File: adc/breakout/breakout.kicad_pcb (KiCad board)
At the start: 2 copper layers, 34.4 x 22.1 mm, 52 parts, among them J1 Conn_01x05_Pin, J2 Conn_01x05_Pin, J3 Conn_01x03_Pin, J4 Conn_01x06_Pin, U1 ESD5344D-TP, U2 ADS1261IRHBR, U3 ESD5344D-TP, U4 ESD5344D-TP

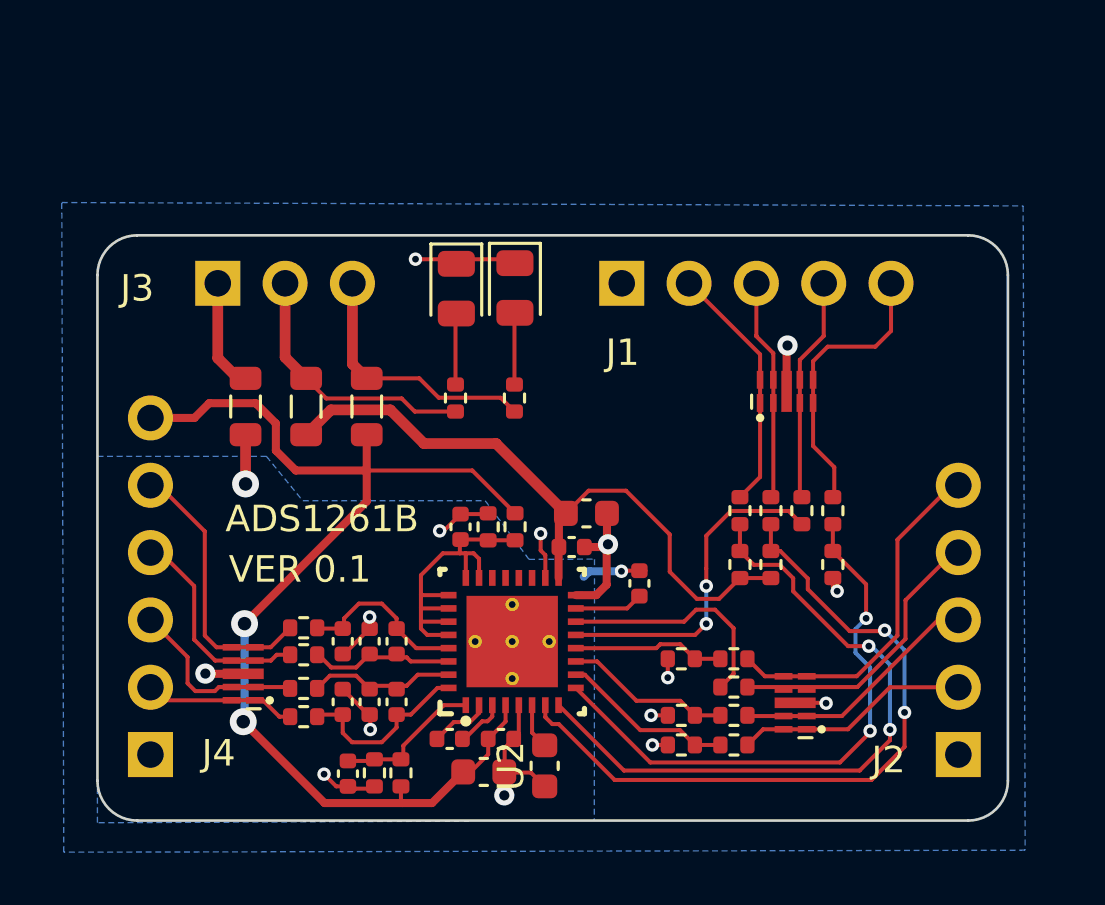
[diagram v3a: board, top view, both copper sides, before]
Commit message: Completed the layout of the power supplies.
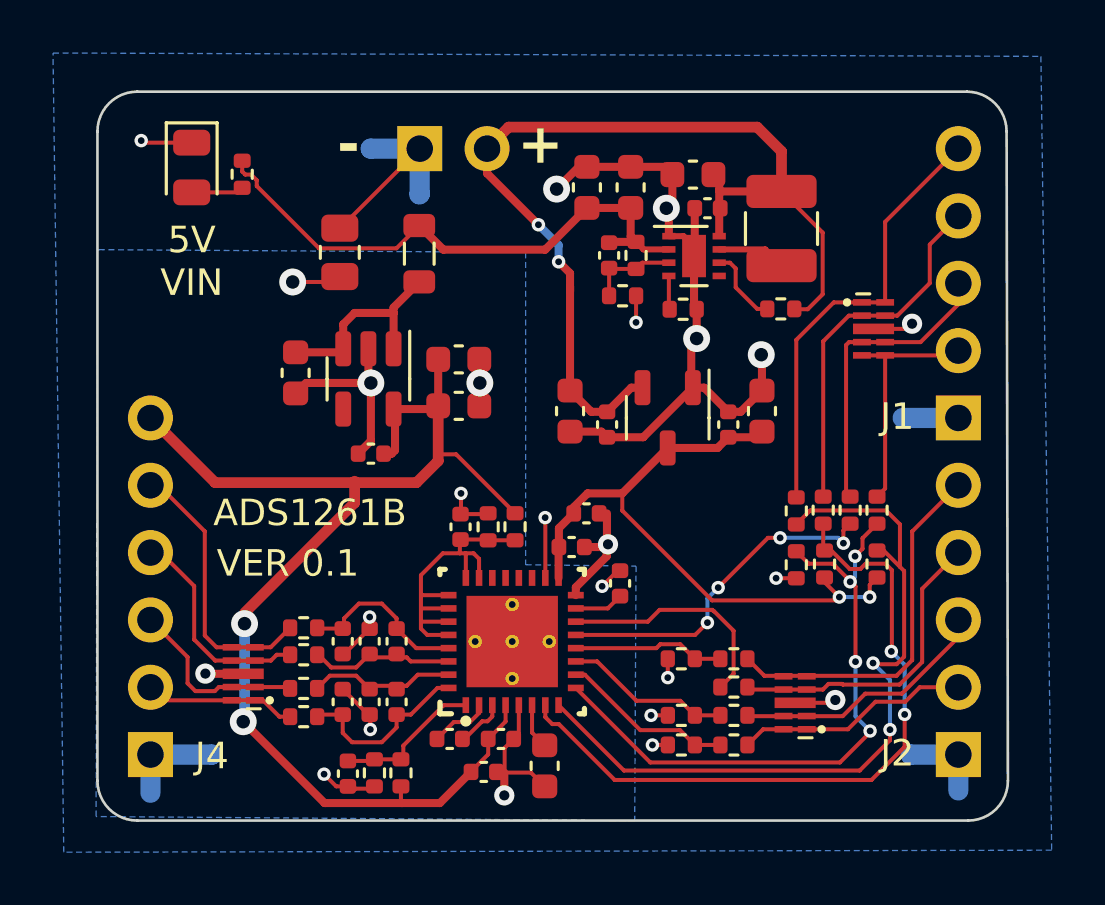
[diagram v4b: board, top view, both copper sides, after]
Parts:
- removed D2: YELLOW, LED_SMD:LED_0805_2012Metric
- removed FB1, FB2, FB3: Ferrite Bead, Inductor_SMD:L_0805_2012Metric
- removed R22: 2K4, Resistor_SMD:R_0402_1005Metric
- added C16: 10u, Capacitor_SMD:C_0603_1608Metric, F.Cu at (22.5, -24.4)
- added C17: 10u, Capacitor_SMD:C_0603_1608Metric, F.Cu at (7.48, -16.9)
- added C18: 100pf, Capacitor_SMD:C_0402_1005Metric, F.Cu at (19.3, -21.3)
- added C19: 100n, Capacitor_SMD:C_0402_1005Metric, F.Cu at (23.0, -23.1)
- added C20: 10u, Capacitor_SMD:C_0603_1608Metric, F.Cu at (20.1, -23.9)
- added C21: 10u, Capacitor_SMD:C_0603_1608Metric, F.Cu at (13.6, -17.4)
- added C22: 100n, Capacitor_SMD:C_0402_1005Metric, F.Cu at (10.3, -13.8)
- added C23: 10u, Capacitor_SMD:C_0603_1608Metric, F.Cu at (13.6, -15.6)
- added C24: 100n, Capacitor_SMD:C_0402_1005Metric, F.Cu at (23.8, -14.9)
- added C25: 10u, Capacitor_SMD:C_0603_1608Metric, F.Cu at (25.1, -15.4)
- added C26: 100n, Capacitor_SMD:C_0402_1005Metric, F.Cu at (19.2, -14.9)
- added C27: 10u, Capacitor_SMD:C_0603_1608Metric, F.Cu at (17.8, -15.4)
- added C28: 10u, Capacitor_SMD:C_0603_1608Metric, F.Cu at (18.5, -23.9)
- added FB5: Ferrite Bead, Inductor_SMD:L_0805_2012Metric, F.Cu at (12.1, -21.4)
- added L1: 1uH, Inductor_SMD:L_1210_3225Metric, F.Cu at (25.8, -22.3)
- added R11: 536K, Resistor_SMD:R_0402_1005Metric, F.Cu at (20.3, -21.3)
- added R13: 150K, Resistor_SMD:R_0402_1005Metric, F.Cu at (19.8, -19.8)
- added R15: 3K3, Resistor_SMD:R_0402_1005Metric, F.Cu at (5.46, -24.4)
- added R7: 100K, Resistor_SMD:R_0402_1005Metric, F.Cu at (25.8, -19.3)
- added R9: 20K, Resistor_SMD:R_0402_1005Metric, F.Cu at (22.1, -19.3)
- added U5: TPS7A2050PDBVR, Package_TO_SOT_SMD:SOT-23-5, F.Cu at (10.2, -16.7)
- added U6: TPS61252DSG, Package_SON:WSON-8-1EP_2x2mm_P0.5mm_EP0.9x1.6mm, F.Cu at (22.5, -21.3)
- added U7: XC6206P332MR, Package_TO_SOT_SMD:SOT-23-3, F.Cu at (21.5, -15.2)
- C1, C2: value 10u -> 1u; footprint Capacitor_SMD:C_0603_1608Metric -> Capacitor_SMD:C_0402_1005Metric
- C3, C4: value 1u -> 100n
- J3: footprint breakout:PinHeader_1x03_P2.54mm_Vertical -> breakout:PinHeader_1x02_P2.54mm_Vertical
- R21: value 2K4 -> 0R; footprint Resistor_SMD:R_0402_1005Metric -> Resistor_SMD:R_0805_2012Metric
- moved J1 13.7 mm to (32.5, -15.2), turned to 180 degrees
- moved D1 13.0 mm to (3.56, -24.6)
- moved J3 9.16 mm to (12.2, -25.4)
- moved R21 8.58 mm to (9.14, -21.4), turned to -90 degrees
- moved R4 5.17 mm to (29.4, -9.68)
- moved R8 5.17 mm to (29.4, -11.7)
- moved U1 4.04 mm to (29.3, -18.6), turned to 0 degrees
- moved R10 2.99 mm to (28.4, -11.7)
- moved R5 2.02 mm to (27.4, -9.68)
- moved R14 1.38 mm to (26.4, -11.7)
- moved R16 1.38 mm to (26.4, -9.65)
- moved R12 0.81 mm to (27.4, -11.7)
- moved C7 0.73 mm to (19.7, -8.95)
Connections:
- net /IN0 renamed Net-(J4-Pin_2)
- net /IN1 renamed Net-(J4-Pin_3)
- net /IN2 renamed Net-(J4-Pin_4)
- net /IN3 renamed Net-(J4-Pin_5)
- J3 pad 2: /3V3_LED -> Net-(J3-Pin_2)
- R10 pad 2: Net-(U2-PWDN_N) -> Net-(U2-DRDY_N)
- R12 pad 2: Net-(U2-DRDY_N) -> Net-(U2-PWDN_N)
- R14 pad 2: Net-(U2-START) -> Net-(U2-RESET_N)
- R21 pad 1: /5V_LED -> GNDD
- R21 pad 2: Net-(D1-A) -> GNDA
- R8 pad 2: Net-(U2-RESET_N) -> Net-(U2-START)
- U1 pad 1: Net-(J1-Pin_2) -> Net-(J1-Pin_5)
- U1 pad 2: Net-(J1-Pin_3) -> Net-(J1-Pin_4)
- U1 pad 4: Net-(J1-Pin_4) -> Net-(J1-Pin_3)
- U1 pad 5: Net-(J1-Pin_5) -> Net-(J1-Pin_2)
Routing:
- net Net-(J3-Pin_2): track 0.00 -> 39.1 mm, vias 0 -> 2
- net GNDD: track 20.4 -> 55.3 mm, vias 9 -> 14
- net Net-(U6-VOUT): track 0.00 -> 21.5 mm
- net GNDA: track 18.6 -> 29.9 mm, vias 8 -> 10
- net /3V3_LED: track 10.1 -> 0.00 mm
- net /5V_LED: track 9.90 -> 0.00 mm
- net Net-(U5-EN): track 0.00 -> 7.78 mm
- net Net-(J1-Pin_5): track 10.7 -> 16.8 mm
- net +5VA: track 42.8 -> 48.2 mm
- net Net-(J1-Pin_4): track 8.65 -> 14.1 mm
- net Net-(U2-RESET_N): track 25.6 -> 29.0 mm
- net Net-(U6-FB): track 0.00 -> 3.41 mm
- net Net-(J1-Pin_3): track 8.44 -> 11.4 mm
- net Net-(U6-EN): track 0.00 -> 2.95 mm
- net Net-(D2-A): track 2.76 -> 0.00 mm
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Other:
- board size 34.4 x 22.1 mm -> 34.4 x 27.5 mm
- board text added: "+"
- board text added: "-"
- board text added: "5V VIN"

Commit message: Minor tweaks of the silkscreen layer.
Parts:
- U5: footprint Package_TO_SOT_SMD:SOT-23-5 -> breakout:SOT-23-5
- U6: footprint Package_SON:WSON-8-1EP_2x2mm_P0.5mm_EP0.9x1.6mm -> breakout:WSON-8-1EP_2x2mm_P0.5mm_EP0.9x1.6mm

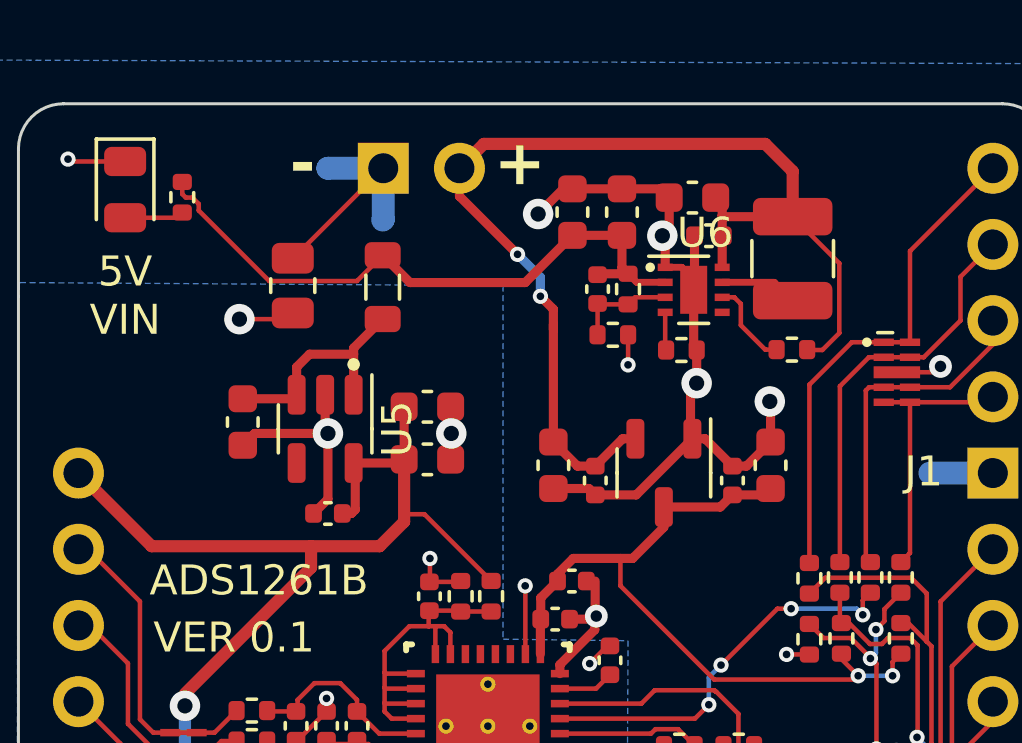
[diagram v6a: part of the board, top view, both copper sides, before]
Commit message: Fixed pinout of 3.3V regulator. Final touches.
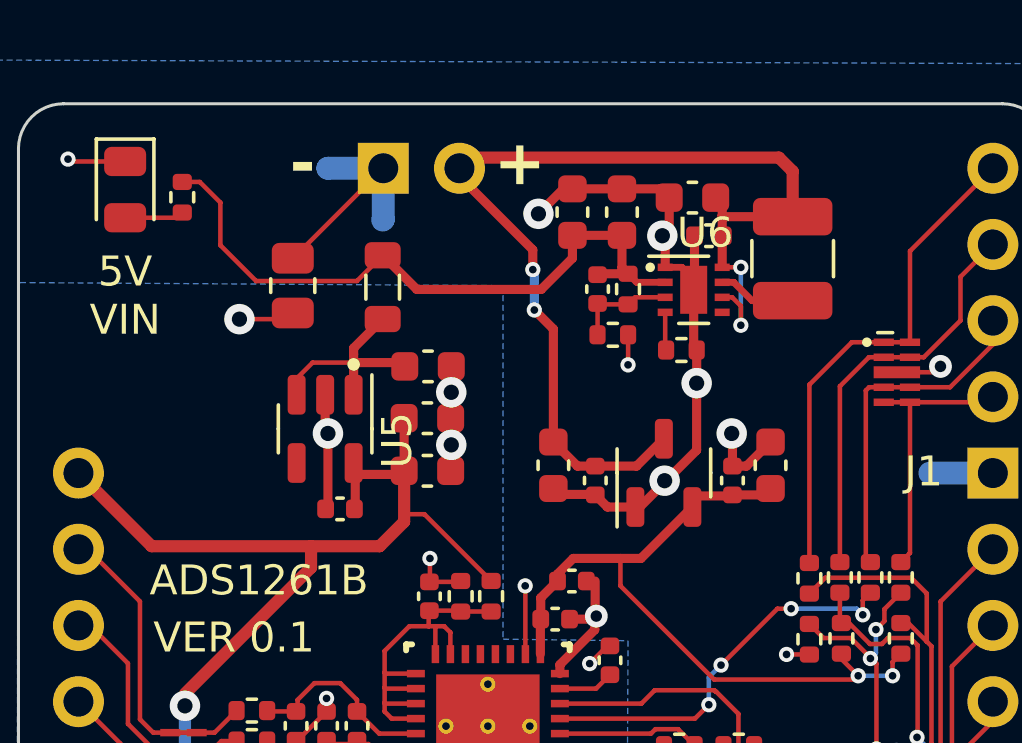
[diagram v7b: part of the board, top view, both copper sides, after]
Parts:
- removed R7: 100K, Resistor_SMD:R_0402_1005Metric
- moved C17 6.45 mm to (13.7, -18.7), turned to 180 degrees
- moved C22 0.43 mm to (10.7, -14.0)
- moved C21 0.38 mm to (13.6, -17.0)
- moved C23 0.38 mm to (13.6, -15.3)
- turned U7 to 90 degrees
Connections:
- U6 pad 6: Net-(U6-EN) -> Net-(J3-Pin_2)
- U7 pad 2: Net-(J3-Pin_2) -> +3V3
- U7 pad 3: +3V3 -> Net-(J3-Pin_2)
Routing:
- net GNDA: track 29.9 -> 24.8 mm, vias 10 -> 11
- net Net-(U6-EN): track 2.95 -> 0.00 mm
- net GNDD: track 55.3 -> 53.7 mm, vias 14 -> 15
- net Net-(J3-Pin_2): track 39.1 -> 37.6 mm, vias 2 -> 4
- net Net-(U6-VOUT): track 21.5 -> 22.6 mm
- net +5VA: track 48.2 -> 47.3 mm
- net +3V3: track 24.7 -> 24.1 mm
